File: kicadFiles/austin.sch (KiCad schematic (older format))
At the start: 475 parts, among them J1 TYPE-C-31-M12_13, J2 Conn_01x04_Male, J5 Conn_01x06_Male, Q1 AO4406AL, SW1 MXSwitch, SW10 MXSwitch, SW100 MXSwitch, SW101 MXSwitch, SW102 MXSwitch, SW103 MXSwitch, SW104 MXSwitch, SW105 MXSwitch, SW106 MXSwitch, SW107 MXSwitch, SW108 MXSwitch, SW109 MXSwitch, SW11 MXSwitch, SW110 MXSwitch, SW111 MXSwitch, SW112 MXSwitch, SW113 MXSwitch, SW114 MXSwitch, SW12 MXSwitch, SW13 MXSwitch, SW14 MXSwitch, SW15 MXSwitch, SW16 MXSwitch, SW17 MXSwitch, SW18 MXSwitch, SW19 MXSwitch, SW2 MXSwitch, SW20 MXSwitch, SW21 MXSwitch, SW22 MXSwitch, SW23 MXSwitch, SW24 MXSwitch, SW25 MXSwitch, SW26 MXSwitch, SW27 MXSwitch, SW28 MXSwitch, SW29 MXSwitch, SW3 MXSwitch, SW30 MXSwitch, SW31 MXSwitch, SW32 MXSwitch, SW33 MXSwitch, SW34 MXSwitch, SW35 MXSwitch, SW36 MXSwitch, SW37 MXSwitch, SW38 MXSwitch, SW39 MXSwitch, SW4 MXSwitch, SW40 MXSwitch, SW41 MXSwitch, SW42 MXSwitch, SW43 MXSwitch, SW44 MXSwitch, SW45 MXSwitch, SW46 MXSwitch, SW47 MXSwitch, SW48 MXSwitch, SW49 MXSwitch, SW5 MXSwitch, SW50 MXSwitch, SW51 MXSwitch, SW52 MXSwitch, SW53 MXSwitch, SW54 MXSwitch, SW55 MXSwitch, SW56 MXSwitch, SW57 MXSwitch, SW59 MXSwitch, SW6 MXSwitch, SW60 MXSwitch, SW61 MXSwitch, SW62 MXSwitch, SW63 MXSwitch, SW64 MXSwitch, SW65 MXSwitch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

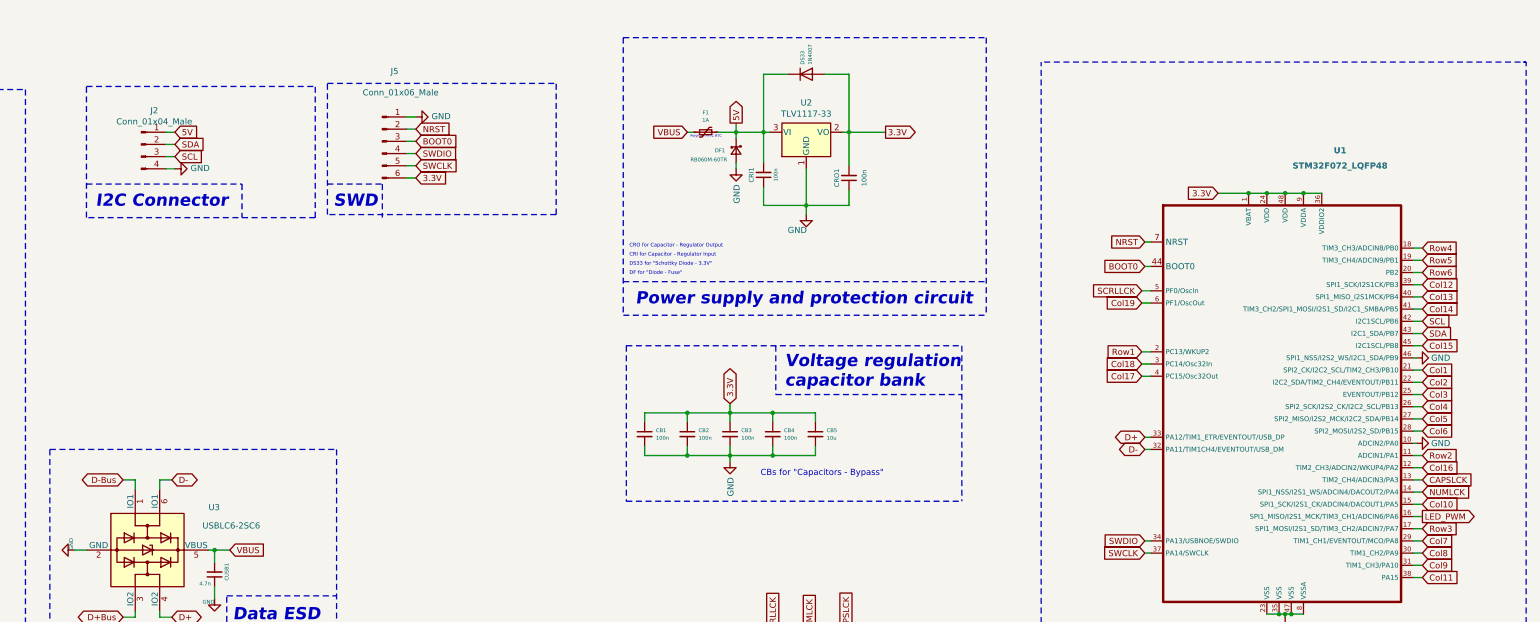
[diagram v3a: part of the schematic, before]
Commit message: [Update] Re-assigned LED pins. Removed I2C pin header breakouts.
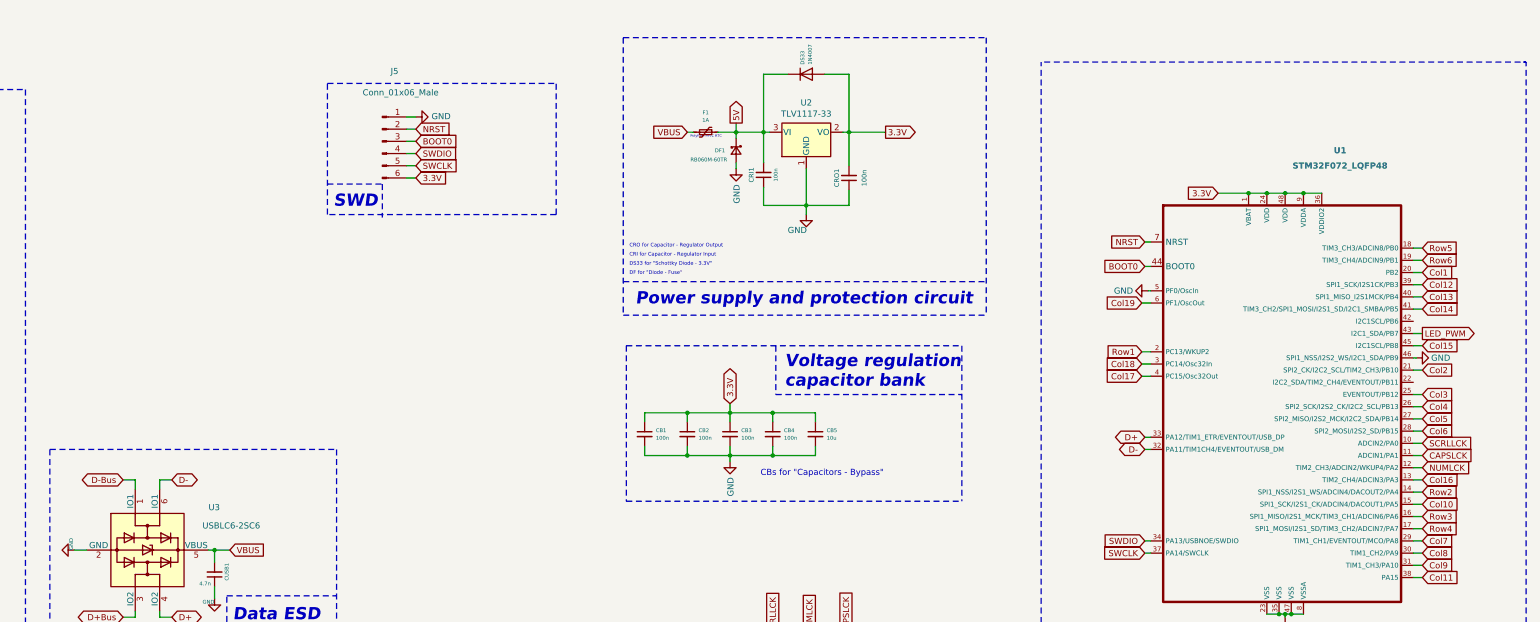
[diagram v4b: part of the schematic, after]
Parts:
- removed J2: Conn_01x04_Male, acheronConnectors:HEADER_4PIN, symbol Connector:Conn_01x04_Male
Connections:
- net SDA is gone; now on net LED_PWM: U1.43 (I2C1_SDA/PB7)
- net CAPSLCK: now also U1.11 (ADCIN1/PA1); no longer U1.13 (TIM2_CH4/ADCIN3/PA3)
- net Col1: now also U1.20 (PB2); no longer U1.21 (SPI2_CK/I2C2_SCL/TIM2_CH3/PB10)
- net Col16: now also U1.13 (TIM2_CH4/ADCIN3/PA3); no longer U1.12 (TIM2_CH3/ADCIN2/WKUP4/PA2)
- net Col2: now also U1.21 (SPI2_CK/I2C2_SCL/TIM2_CH3/PB10); no longer U1.22 (I2C2_SDA/TIM2_CH4/EVENTOUT/PB11)
- net GND: now also U1.5 (PF0/OscIn); no longer U1.10 (ADCIN2/PA0)
- net LED_PWM: no longer U1.16 (SPI1_MISO/I2S1_MCK/TIM3_CH1/ADCIN6/PA6)
- net NUMLCK: now also U1.12 (TIM2_CH3/ADCIN2/WKUP4/PA2); no longer U1.14 (SPI1_NSS/I2S1_WS/ADCIN4/DACOUT2/PA4)
- net Row2: now also U1.14 (SPI1_NSS/I2S1_WS/ADCIN4/DACOUT2/PA4); no longer U1.11 (ADCIN1/PA1)
- net Row3: now also U1.16 (SPI1_MISO/I2S1_MCK/TIM3_CH1/ADCIN6/PA6); no longer U1.17 (SPI1_MOSI/I2S1_SD/TIM3_CH2/ADCIN7/PA7)
- net Row4: now also U1.17 (SPI1_MOSI/I2S1_SD/TIM3_CH2/ADCIN7/PA7); no longer U1.18 (TIM3_CH3/ADCIN8/PB0)
- net Row5: now also U1.18 (TIM3_CH3/ADCIN8/PB0); no longer U1.19 (TIM3_CH4/ADCIN9/PB1)
- net Row6: now also U1.19 (TIM3_CH4/ADCIN9/PB1); no longer U1.20 (PB2)
- net SCRLLCK: now also U1.10 (ADCIN2/PA0); no longer U1.5 (PF0/OscIn)
- net SCL: no longer names the net of U1.42 (I2C1SCL/PB6)
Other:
- note removed: "I2C Connector"
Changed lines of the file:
@@
 Text GLabel 7925 15125 0    50   Input ~ 0
 3.3V
-Text GLabel 21650 12775 2    50   Input ~ 0
+Text GLabel 21650 12675 2    50   Input ~ 0
 Row3
-Text GLabel 21650 12175 2    50   Input ~ 0
+Text GLabel 21650 12475 2    50   Input ~ 0
 Row2
 Wire Wire Line
-	21650 12175 21575 12175
-Text GLabel 21650 10475 2    50   Input ~ 0
+	21650 12475 21575 12475
+Text GLabel 21650 12775 2    50   Input ~ 0
 Row4
 Wire Wire Line
-	21650 10475 21575 10475
-Wire Wire Line
 	21650 12775 21575 12775
 Wire Wire Line
+	21650 12675 21575 12675
+Wire Wire Line
 	21650 12975 21575 12975
 Text GLabel 21650 13175 2    50   Input ~ 0
@@
 Wire Notes Line width 20
 	15100 11025 18075 11025
-$Comp
-L Connector:Conn_01x04_Male J2
-U 1 1 5C8FE384
-P 11150 9625
-F 0 "J2" H 11256 9903 50  0000 C CNN
-F 1 "Conn_01x04_Male" H 11256 9812 50  0000 C CNN
-F 2 "acheronConnectors:HEADER_4PIN" H 11150 9625 50  0001 C CNN
-F 3 "~" H 11150 9625 50  0001 C CNN
-	1    11150 9625
-	1    0    0    -1
-$EndComp
-Wire Wire Line
-	11350 9525 11425 9525
-Text GLabel 11425 9525 2    50   Input ~ 0
-5V
-Wire Wire Line
-	11350 9825 11425 9825
-$Comp
-L power:GND #PWR0102
-U 1 1 5C9D3CEB
-P 11425 9825
-F 0 "#PWR0102" H 11425 9575 50  0001 C CNN
-F 1 "GND" V 11430 9697 50  0000 R CNN
-F 2 "" H 11425 9825 50  0001 C CNN
-F 3 "" H 11425 9825 50  0001 C CNN
-	1    11425 9825
-	0    -1   -1   0
-$EndComp
-Wire Wire Line
-	11350 9625 11425 9625
-Text GLabel 11425 9625 2    50   Input ~ 0
-SDA
-Text GLabel 11425 9725 2    50   Input ~ 0
-SCL
-Wire Wire Line
-	11425 9725 11350 9725
-Wire Notes Line width 20
-	10700 9150 12575 9150
-Wire Notes Line width 20
-	12575 10225 10700 10225
-Text Notes 10775 10150 0    100  Italic 20
-I2C Connector
-Text GLabel 21650 11075 2    50   Input ~ 0
-SCL
-Text GLabel 21650 11175 2    50   Input ~ 0
-SDA
-Wire Wire Line
-	21650 11075 21575 11075
-Wire Wire Line
-	21575 11175 21650 11175
-Wire Notes Line width 20
-	12575 10225 12575 9150
-Wire Notes Line width 20
-	10700 10225 10700 9150
 Wire Notes Line width 20
 	10225 14125 10225 15850
@@
 	1    0    0    -1
 $EndComp
-Text GLabel 21650 11575 2    50   Input ~ 0
+Text GLabel 21650 11475 2    50   Input ~ 0
 Col2
 Text GLabel 21650 11675 2    50   Input ~ 0
@@
 	21650 11675 21575 11675
 Wire Wire Line
-	21650 11575 21575 11575
+	21650 11475 21575 11475
 Text GLabel 21650 10975 2    50   Input ~ 0
 Col14
@@
 Wire Wire Line
 	19350 10925 19425 10925
-Text GLabel 21650 10575 2    50   Input ~ 0
+Text GLabel 21650 10475 2    50   Input ~ 0
 Row5
 Wire Wire Line
-	21650 10575 21575 10575
+	21650 10475 21575 10475
 Wire Wire Line
 	11300 13500 11400 13500
@@
 Col12
 Wire Wire Line
-	21650 10675 21575 10675
-Text GLabel 21650 10675 2    50   Input ~ 0
+	21650 10575 21575 10575
+Text GLabel 21650 10575 2    50   Input ~ 0
 Row6
 Text Notes 16225 12350 0    50   ~ 0
@@
 Text GLabel 21650 12875 2    50   Input ~ 0
 Col7
-Text GLabel 21650 12275 2    50   Input ~ 0
+Text GLabel 21650 12375 2    50   Input ~ 0
 Col16
 Wire Wire Line
-	21650 12275 21575 12275
+	21650 12375 21575 12375
 Text GLabel 21650 11775 2    50   Input ~ 0
 Col4
@@
 Col13
 Wire Wire Line
-	21650 12675 21575 12675
-Text GLabel 21650 12675 2    50   Output ~ 0
+	21650 11175 21575 11175
+Text GLabel 21650 11175 2    50   Output ~ 0
 LED_PWM
 Wire Wire Line
-	21650 11475 21575 11475
-Text GLabel 21650 11475 2    50   Input ~ 0
+	21650 10675 21575 10675
+Text GLabel 21650 10675 2    50   Input ~ 0
 Col1
 $Comp
@@
 Text Notes 3750 13500 0    50   ~ 0
 RGP for "Gate Parallel"\nRGS for "Gate Series"
-Text GLabel 19350 10825 0    50   Input ~ 0
+Text GLabel 21650 12075 2    50   Input ~ 0
 SCRLLCK
 Wire Wire Line
-	19350 10825 19425 10825
-Text GLabel 21650 12375 2    50   Input ~ 0
+	21650 12075 21575 12075
+Text GLabel 21650 12175 2    50   Input ~ 0
 CAPSLCK
 Wire Wire Line
-	21575 12375 21650 12375
+	21575 12175 21650 12175
 Wire Wire Line
-	21650 12475 21575 12475
-Text GLabel 21650 12475 2    50   Input ~ 0
+	21650 12275 21575 12275
+Text GLabel 21650 12275 2    50   Input ~ 0
 NUMLCK
 $Comp
@@
 $EndComp
 $Comp
-L power:GND #PWR0109
-U 1 1 5D2771A8
-P 21600 12075
-F 0 "#PWR0109" H 21600 11825 50  0001 C CNN
-F 1 "GND" V 21600 11875 50  0000 C CNN
-F 2 "" H 21600 12075 50  0001 C CNN
-F 3 "" H 21600 12075 50  0001 C CNN
-	1    21600 12075
-	0    -1   -1   0
-$EndComp
-$Comp
 L power:GND #PWR0110
 U 1 1 5D37D0BF
@@
 Wire Wire Line
 	21600 11375 21575 11375
-Wire Wire Line
-	21600 12075 21575 12075
 Wire Notes Line width 20
 	1250 7700 3050 7700
@@
 $EndComp
 Wire Notes Line width 20
-	10700 9950 11975 9950
-Wire Notes Line width 20
-	11975 9950 11975 10225
-Wire Notes Line width 20
 	12675 9950 13125 9950
 Wire Notes Line width 20
@@
 	1    0    0    -1
 $EndComp
+$Comp
+L power:GND #PWR0109
+U 1 1 5DCDF6A1
+P 19400 10825
+F 0 "#PWR0109" H 19400 10575 50  0001 C CNN
+F 1 "GND" V 19400 10625 50  0000 C CNN
+F 2 "" H 19400 10825 50  0001 C CNN
+F 3 "" H 19400 10825 50  0001 C CNN
+	1    19400 10825
+	0    1    1    0
+$EndComp
+Wire Wire Line
+	19400 10825 19425 10825
 $EndSCHEMATC

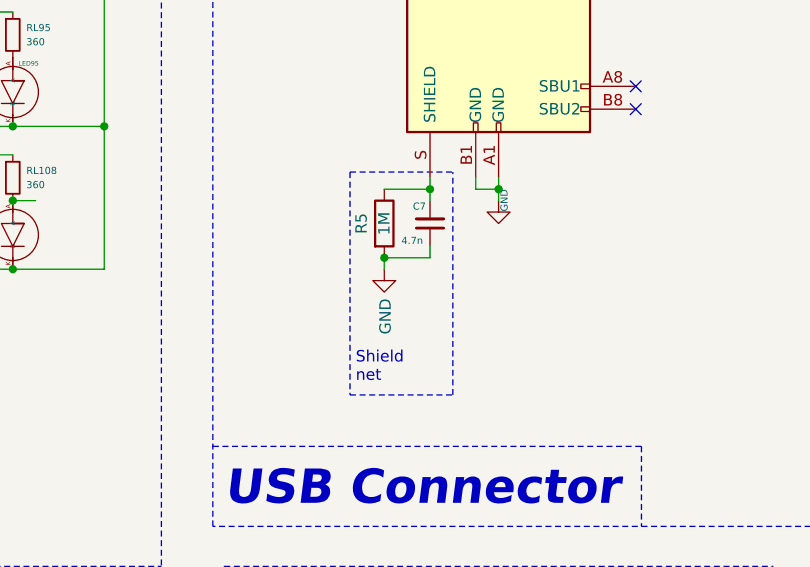
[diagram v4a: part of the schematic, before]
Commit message: [Update] Renamed C7 and R5 to RSH1 and CSH1, updated gerbers
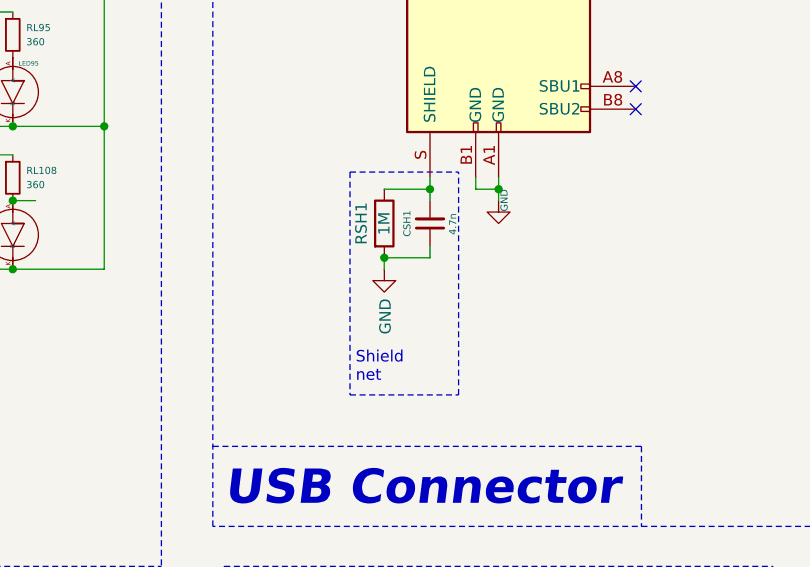
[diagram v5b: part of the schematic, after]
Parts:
- renumbered C7 to CSH1, R5 to RSH1
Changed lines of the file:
@@
 	8325 12275 8325 12325
 $Comp
-L Device:C_Small C7
+L Device:C_Small CSH1
 U 1 1 5C192852
 P 8325 12475
-F 0 "C7" H 8400 12400 31  0000 R CNN
-F 1 "4.7n" H 8450 12550 31  0000 R CNN
+F 0 "CSH1" V 8425 12475 31  0000 C CNN
+F 1 "4.7n" V 8225 12525 31  0000 R CNN
 F 2 "Capacitor_SMD:C_0805_2012Metric_Pad1.15x1.40mm_HandSolder" H 8325 12475 50  0001 C CNN
 F 3 "~" H 8325 12475 50  0001 C CNN
@@
 $EndComp
 $Comp
-L Device:R R5
+L Device:R RSH1
 U 1 1 5C1953C2
 P 8125 12475
-F 0 "R5" V 8025 12475 50  0000 C CNN
+F 0 "RSH1" V 8025 12475 50  0000 C CNN
 F 1 "1M" V 8125 12475 50  0000 C CNN
 F 2 "acheronComponents:R_SMD_1026" V 8055 12475 50  0001 C CNN
@@
 Shield\nnet
 Wire Notes Line
-	8425 13225 8425 12250
+	8450 13225 8450 12250
 Wire Notes Line
 	7975 12250 7975 13225
@@
 Wire Wire Line
 	9275 10175 9325 10175
-Wire Notes Line
-	7975 13225 8425 13225
-Wire Notes Line
-	7975 12250 8425 12250
 Text GLabel 11875 12950 2    50   Input ~ 0
 VBUS
@@
 Wire Wire Line
 	19400 10825 19425 10825
+Wire Notes Line
+	7975 12250 8450 12250
+Wire Notes Line
+	7975 13225 8450 13225
 $EndSCHEMATC

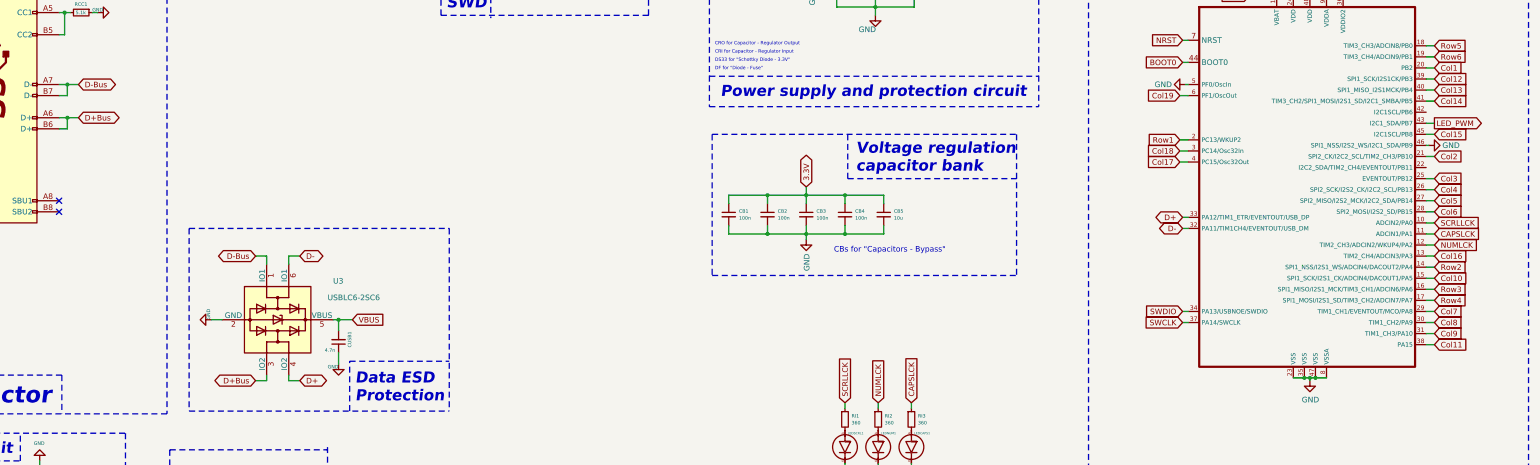
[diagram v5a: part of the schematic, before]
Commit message: [Update] Finished re-routing the connector area, ran DRC
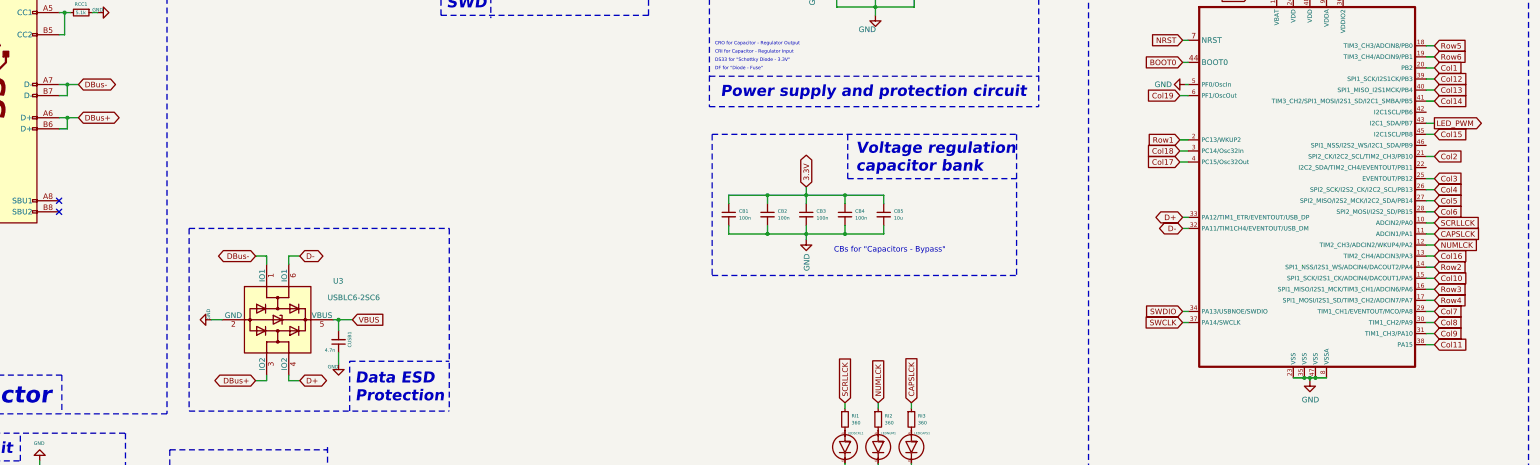
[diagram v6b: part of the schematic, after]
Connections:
- net GND: no longer U1.46 (SPI1_NSS/I2S2_WS/I2C1_SDA/PB9)
- net D+Bus renamed DBus+
- net D-Bus renamed DBus-
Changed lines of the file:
@@
 $EndComp
 Text GLabel 11000 13500 0    50   BiDi ~ 0
-D+Bus
+DBus+
 Wire Wire Line
 	11000 13500 11100 13500
@@
 	11100 12375 11000 12375
 Text GLabel 11000 12375 0    50   BiDi ~ 0
-D-Bus
+DBus-
 $Comp
 L Device:C_Small CUSB1
@@
 	9225 10825 9300 10825
 Text GLabel 9400 11125 2    50   BiDi ~ 0
-D+Bus
+DBus+
 Text GLabel 9400 10825 2    50   BiDi ~ 0
-D-Bus
+DBus-
 Wire Wire Line
 	9300 11125 9400 11125
@@
 	1    0    0    -1
 $EndComp
-$Comp
-L power:GND #PWR0110
-U 1 1 5D37D0BF
-P 21600 11375
-F 0 "#PWR0110" H 21600 11125 50  0001 C CNN
-F 1 "GND" V 21600 11175 50  0000 C CNN
-F 2 "" H 21600 11375 50  0001 C CNN
-F 3 "" H 21600 11375 50  0001 C CNN
-	1    21600 11375
-	0    -1   -1   0
-$EndComp
-Wire Wire Line
-	21600 11375 21575 11375
 Wire Notes Line width 20
 	1250 7700 3050 7700
